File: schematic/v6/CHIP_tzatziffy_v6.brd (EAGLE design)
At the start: 40.9 x 49.8 mm, 50 parts, among them J1 2X20-CHIP0.8_DRILL, J3 S2B-PH-SM4-TB, Q1 NPN-DTC114YUA, Q2 PNP-DTA114YUA, U1 LMR62421, U3 DS2431P, X1 FH12-40S-0.5SH

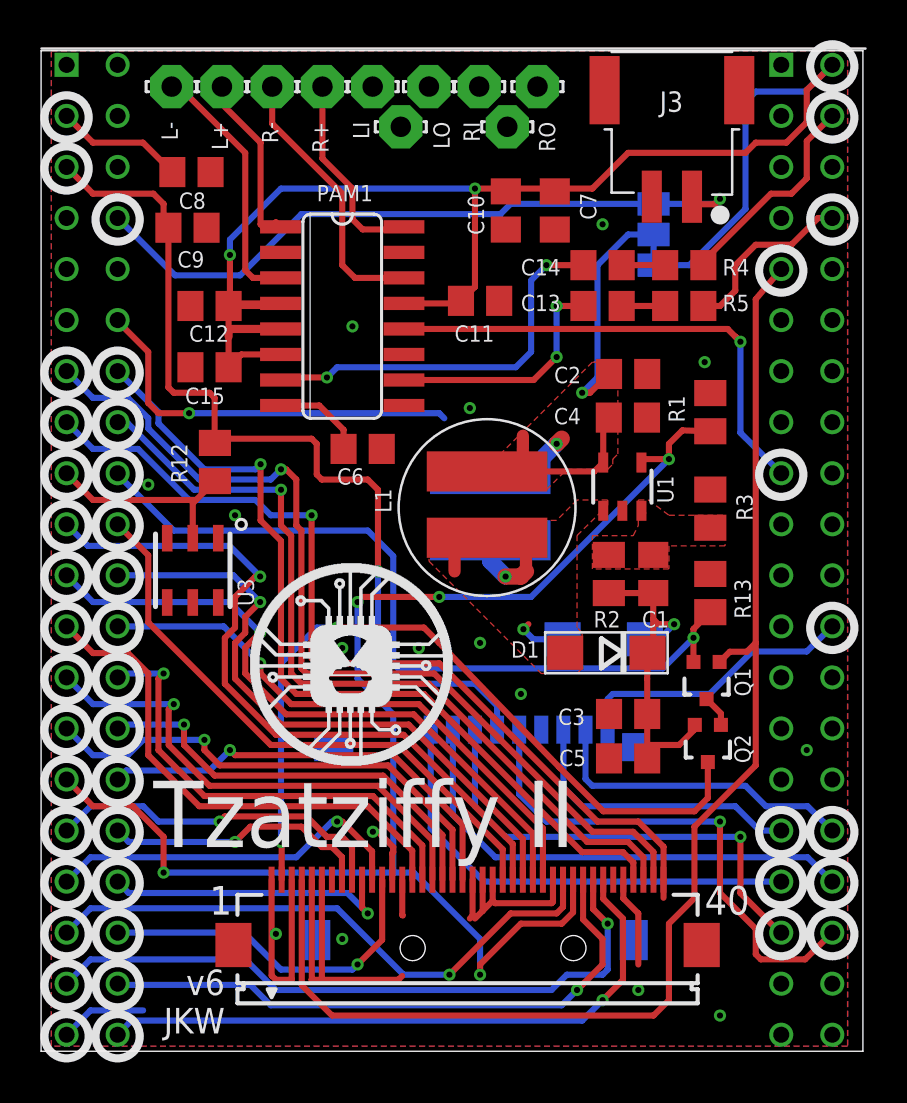
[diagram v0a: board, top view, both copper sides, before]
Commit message: Added connection for poti
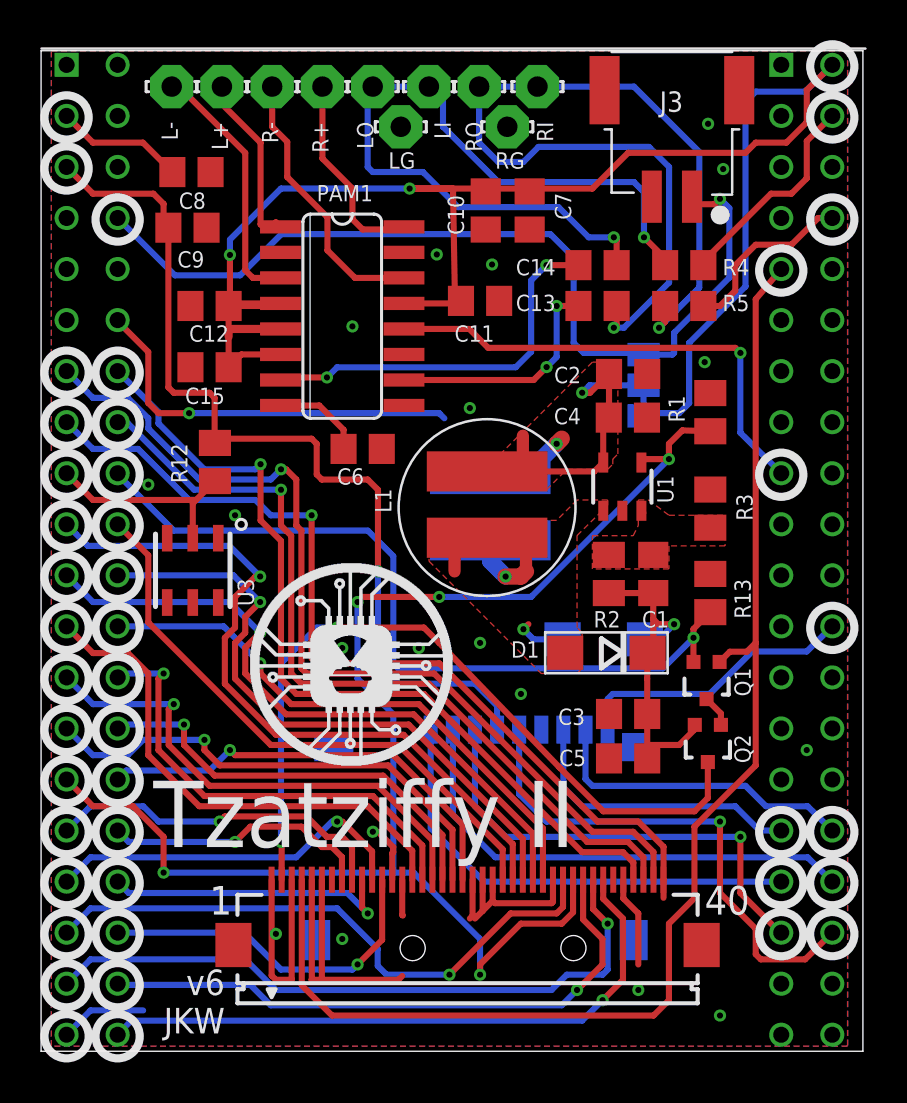
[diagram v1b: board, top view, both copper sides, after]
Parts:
- moved SJ1 7.52 mm to (30.0, 33.1)
- moved RI 2.90 mm to (24.7, 48.0)
- moved RO 2.90 mm to (21.8, 48.0)
- moved LI 2.80 mm to (19.3, 48.0)
- moved LO 2.80 mm to (16.5, 48.0)
- moved C7 1.25 mm to (24.3, 41.8)
- moved C10 1.00 mm to (22.1, 41.8)
- moved C13 0.25 mm to (27.7, 37.1)
- moved C14 0.25 mm to (27.7, 39.1)
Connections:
- removed net N$42: C14.1, R4.1
- removed net PWR_IN: C2.1, C4.1, L1.P$2, L2.P$2, SJ1.2, U1.5
- new net N$43: C13.1, R5.1, RI.MP, RO.MP
- net N$41: now also C14.1, LI.MP, LO.MP, R4.1; no longer C13.1, R5.1
- net VCC5V: now also C2.1, C4.1, L1.P$2, L2.P$2, SJ1.2, U1.5
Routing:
- net N$43: track 0.00 -> 47.0 mm, vias 0 -> 2
- net N$41: track 2.16 -> 39.8 mm, vias 0 -> 2
- net VCC5V: track 77.2 -> 109.5 mm, vias 2 -> 4
- net PWR_IN: track 26.0 -> 0.00 mm, vias 2 -> 0
- net VBAT_EXT: track 34.8 -> 45.8 mm
- net N$42: track 2.16 -> 0.00 mm
- net N$24: track 1.52 -> 0.00 mm
- net GP3: track 24.8 -> 24.1 mm
- net GND: vias 17 -> 20
- added copper zone on layer 1, net VCC5V
- removed copper zone on layer 1, net PWR_IN
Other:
- board text added: "A B"
- board text added: "A:5v (default) B:Battery"

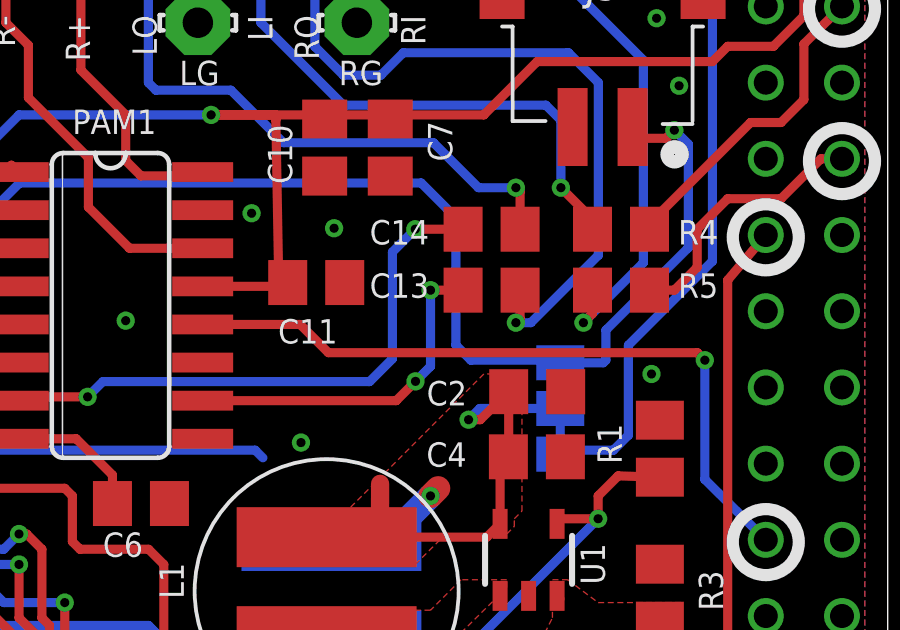
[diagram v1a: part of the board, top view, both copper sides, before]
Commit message: added pulldown for shutdown
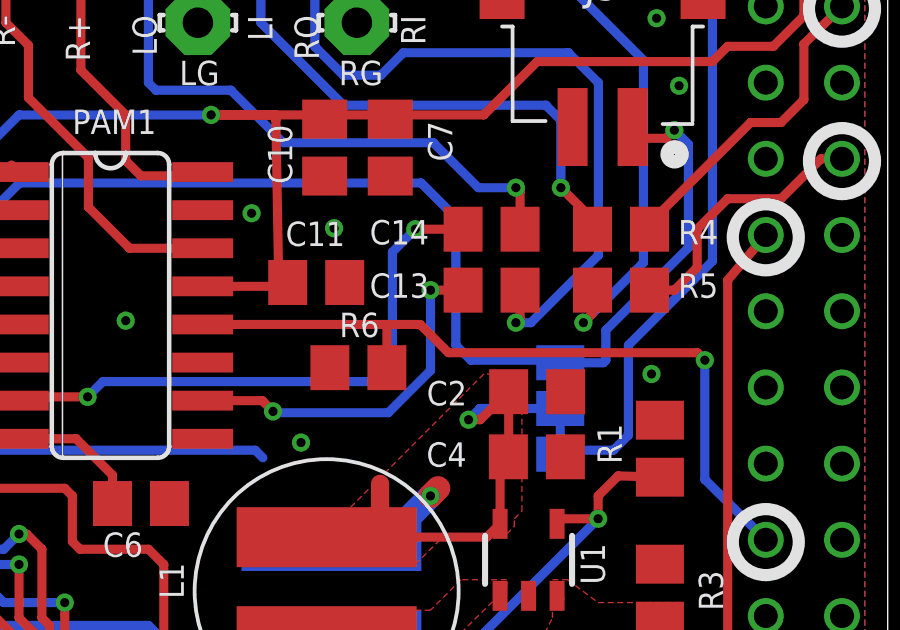
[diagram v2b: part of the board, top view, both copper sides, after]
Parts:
- added R6: n.a., rcl:R0805
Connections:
- net GND: now also R6.1
- net GP3: now also R6.2
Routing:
- net GP3: track 24.1 -> 25.5 mm
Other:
- board text added: "LG"
- board text added: "RG"
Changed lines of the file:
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@@
 <text x="8.382" y="6.8" size="1.4224" layer="25" font="vector">1</text>
 <text x="33.02" y="6.8" size="1.4224" layer="25" font="vector">40</text>
-<text x="6.792" y="46" size="0.8128" layer="22" rot="MR270">L-</text>
-<text x="9.292" y="46" size="0.8128" layer="22" rot="MR270">L+</text>
-<text x="11.792" y="46" size="0.8128" layer="22" rot="MR270">R-</text>
-<text x="14.292" y="46" size="0.8128" layer="22" rot="MR270">R+</text>
+<text x="6.792" y="46" size="0.8128" layer="26" rot="MR270">L-</text>
+<text x="9.292" y="46" size="0.8128" layer="26" rot="MR270">L+</text>
+<text x="11.792" y="46" size="0.8128" layer="26" rot="MR270">R-</text>
+<text x="14.292" y="46" size="0.8128" layer="26" rot="MR270">R+</text>
 <text x="31.496" y="2.794" size="3.3" layer="26" font="vector" ratio="9" rot="MR90">Tzatziffy II</text>
-<text x="20.042" y="46" size="0.8128" layer="22" rot="MR270">Li</text>
-<text x="16.292" y="46" size="0.8128" layer="22" rot="MR270">Lo</text>
-<text x="25.792" y="46" size="0.8128" layer="22" rot="MR270">Ri</text>
-<text x="21.792" y="46" size="0.8128" layer="22" rot="MR270">Ro</text>
+<text x="20.042" y="46" size="0.8128" layer="26" rot="MR270">Li</text>
+<text x="16.292" y="46" size="0.8128" layer="26" rot="MR270">Lo</text>
+<text x="25.792" y="46" size="0.8128" layer="26" rot="MR270">Ri</text>
+<text x="21.792" y="46" size="0.8128" layer="26" rot="MR270">Ro</text>
 <text x="6.936" y="1.606" size="1.27" layer="26" font="vector" ratio="9" rot="MR90">CHIPDIPSHOP</text>
 <text x="28.75" y="34.5" size="1.016" layer="26" font="fixed" rot="MR270">A B</text>
@@
 B:Battery
 </text>
+<wire x1="23.25" y1="49" x2="23.25" y2="47.5" width="0.3048" layer="26"/>
+<wire x1="18" y1="49" x2="18" y2="47.5" width="0.3048" layer="26"/>
+<text x="17.25" y="44.542" size="0.8128" layer="26" rot="MR180">LG</text>
+<text x="22.75" y="44.542" size="0.8128" layer="26" rot="MR180">RG</text>
 </plain>
 <attributes>
@@
 </element>
 <element name="C11" library="rcl" package="C0805" value="1uF" x="21.844" y="37.338" smashed="yes" rot="R180">
-<attribute name="NAME" x="20.574" y="35.306" size="0.8128" layer="25"/>
+<attribute name="NAME" x="20.824" y="38.556" size="0.8128" layer="25"/>
 <attribute name="VALUE" x="23.114" y="39.878" size="1.27" layer="27" rot="R180"/>
 </element>
@@
 <attribute name="VALUE" x="30.64" y="17.944" size="1.2" layer="28" font="vector" ratio="10" rot="MR0"/>
 <attribute name="NAME" x="30.64" y="21.786" size="1.2" layer="156" font="vector" ratio="10" rot="MR0"/>
+</element>
+<element name="R6" library="rcl" package="R0805" value="n.a." x="23.25" y="34.5" smashed="yes">
+<attribute name="NAME" x="22.615" y="35.52" size="0.8128" layer="25"/>
+<attribute name="VALUE" x="22.615" y="31.96" size="1.27" layer="27"/>
 </element>
 </elements>
@@
 <via x="33.94" y="43.898" extent="1-16" drill="0.3048"/>
 <via x="19.69" y="39.648" extent="1-16" drill="0.3048"/>
+<contactref element="R6" pad="1"/>
 </signal>
 <signal name="VREG_OUTPUT">
@@
 <wire x1="34.798" y1="34.75" x2="34.798" y2="30.774" width="0.3048" layer="16"/>
 <wire x1="34.798" y1="30.774" x2="36.83" y2="28.762" width="0.3048" layer="16"/>
-<wire x1="18.0594" y1="35.941" x2="21.309" y2="35.941" width="0.3048" layer="1"/>
-<wire x1="21.309" y1="35.941" x2="22.25" y2="35" width="0.3048" layer="1"/>
-<wire x1="22.25" y1="35" x2="34.548" y2="35" width="0.3048" layer="1"/>
 <wire x1="34.548" y1="35" x2="34.798" y2="34.75" width="0.3048" layer="1"/>
 <via x="34.798" y="34.75" extent="1-16" drill="0.3048"/>
+<contactref element="R6" pad="2"/>
+<wire x1="18.0594" y1="35.941" x2="24.25" y2="35.941" width="0.3048" layer="1"/>
+<wire x1="24.25" y1="35.941" x2="25.309" y2="35.941" width="0.3048" layer="1"/>
+<wire x1="25.309" y1="35.941" x2="26.25" y2="35" width="0.3048" layer="1"/>
+<wire x1="26.25" y1="35" x2="34.548" y2="35" width="0.3048" layer="1"/>
+<wire x1="24.2" y1="34.5" x2="24.2" y2="35.891" width="0.3048" layer="1"/>
+<wire x1="24.2" y1="35.891" x2="24.25" y2="35.941" width="0.3048" layer="1"/>
 </signal>
 <signal name="GP4">
@@
 <contactref element="PAM1" pad="10"/>
 <contactref element="C13" pad="2"/>
-<wire x1="18.0594" y1="33.401" x2="24.511" y2="33.401" width="0.3048" layer="1"/>
-<wire x1="24.511" y1="33.401" x2="25.154" y2="34.044" width="0.3048" layer="1"/>
-<via x="25.154" y="34.044" extent="1-16" drill="0.3048"/>
+<via x="20.404" y="33.044" extent="1-16" drill="0.3048"/>
 <via x="25.654" y="37.084" extent="1-16" drill="0.3048"/>
 <wire x1="25.654" y1="37.084" x2="26.74" y2="37.084" width="0.3048" layer="1"/>
-<wire x1="25.654" y1="37.084" x2="25.654" y2="34.544" width="0.3048" layer="16"/>
-<wire x1="25.654" y1="34.544" x2="25.154" y2="34.044" width="0.3048" layer="16"/>
+<wire x1="25.654" y1="37.084" x2="25.654" y2="34.404" width="0.3048" layer="16"/>
+<wire x1="18.0594" y1="33.401" x2="20.047" y2="33.401" width="0.3048" layer="1"/>
+<wire x1="20.047" y1="33.401" x2="20.404" y2="33.044" width="0.3048" layer="1"/>
+<wire x1="25.654" y1="34.404" x2="24.25" y2="33" width="0.3048" layer="16"/>
+<wire x1="24.25" y1="33" x2="20.448" y2="33" width="0.3048" layer="16"/>
+<wire x1="20.448" y1="33" x2="20.404" y2="33.044" width="0.3048" layer="16"/>
 </signal>
 <signal name="N$40">

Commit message: changed pulldown to assembled
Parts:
- R6: value n.a. -> 12k
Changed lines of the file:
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@@
 <attribute name="NAME" x="30.64" y="21.786" size="1.2" layer="156" font="vector" ratio="10" rot="MR0"/>
 </element>
-<element name="R6" library="rcl" package="R0805" value="n.a." x="23.25" y="34.5" smashed="yes">
+<element name="R6" library="rcl" package="R0805" value="12k" x="23.25" y="34.5" smashed="yes">
 <attribute name="NAME" x="22.615" y="35.52" size="0.8128" layer="25"/>
 <attribute name="VALUE" x="22.615" y="31.96" size="1.27" layer="27"/>
